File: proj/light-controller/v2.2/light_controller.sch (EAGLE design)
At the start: 214 parts, among them J1 0022232051, J2 PJ-036AH, J4 54602-908LF, J5 A-2004-1-4-LP-N-R, J6 A-2004-1-4-LP-N-R, J7 I2C-HEADER, J8 54602-908LF, U1 RCD-24-0.70/VREF, U10 PCA9685, U11 PCA9615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

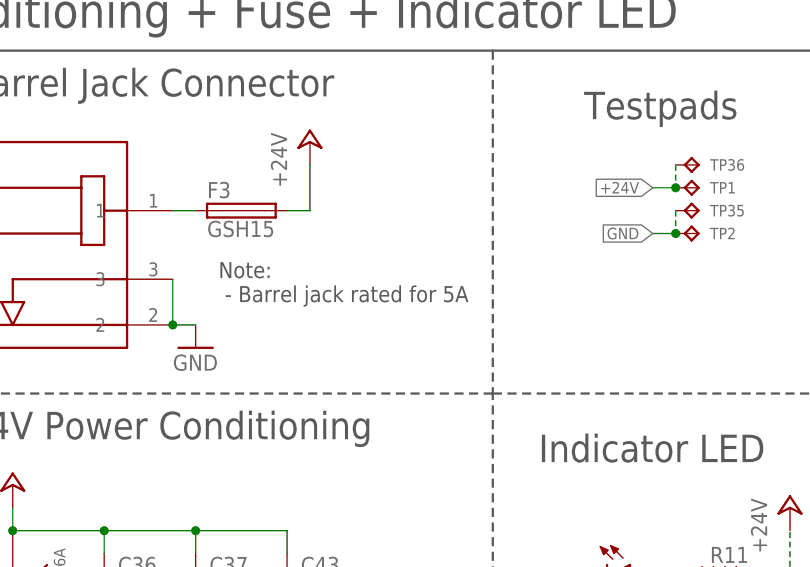
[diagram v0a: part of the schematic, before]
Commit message: added BOM for light controlled v2.2
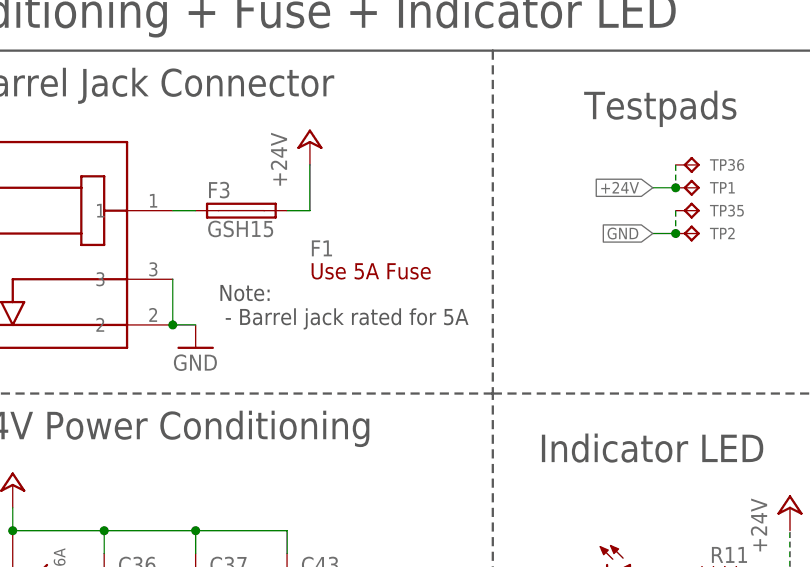
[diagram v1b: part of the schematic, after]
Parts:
- added F1: Use 5A Fuse, openag-fuses:0217005.MXP
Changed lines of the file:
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@@
 <part name="TP37" library="openag-testpads" deviceset="TP" device="TP04R"/>
 <part name="TP38" library="openag-testpads" deviceset="TP" device="TP04R"/>
+<part name="F1" library="openag-fuses" deviceset="0217005.MXP" device="" value="Use 5A Fuse"/>
 </parts>
 <sheets>
@@
 <text x="657.86" y="259.08" size="3.048" layer="97">Testpads</text>
 <wire x1="647.7" y1="266.7" x2="647.7" y2="228.6" width="0.254" layer="97" style="longdash"/>
-<text x="617.22" y="238.76" size="1.778" layer="97">Note:
+<text x="617.22" y="236.22" size="1.778" layer="97">Note:
  - Barrel jack rated for 5A</text>
 <wire x1="266.7" y1="419.1" x2="266.7" y2="342.9" width="0.254" layer="97"/>
@@
 <instance part="TP37" gate="G$1" x="515.62" y="358.14" rot="R180"/>
 <instance part="TP38" gate="G$1" x="515.62" y="363.22" rot="R180"/>
+<instance part="F1" gate="G$1" x="632.46" y="241.3"/>
 </instances>
 <busses>

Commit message: added auto map generation script and applied to light controlled v2.2
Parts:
- U$7: URL https://github.com/openaginitiative/openag_eagle/proj/light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 -> github.com/openaginitiative/openag_eagle/proj/light-control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
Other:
- note added: "Changelog - added particle photon"
- note added: "RJ45 Connector Pair w/dI2C Redriver"
- note removed: "Changelog - added psoc4100"
- note removed: "RJ45 Connector Pair w/dI2C Buffer"
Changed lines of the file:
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@@
 <setting verticaltext="up"/>
 </settings>
-<grid distance="0.1" unitdist="inch" unit="inch" style="lines" multiple="1" display="yes" altdistance="0.01" altunitdist="inch" altunit="inch"/>
+<grid distance="1.5" unitdist="inch" unit="inch" style="lines" multiple="1" display="yes" altdistance="0.01" altunitdist="inch" altunit="inch"/>
 <layers>
 <layer number="1" name="Top" color="4" fill="1" visible="no" active="no"/>
@@
 <part name="U$7" library="openag-frames" deviceset="TITLE" device="">
 <attribute name="TITLE" value="Light Controller"/>
-<attribute name="URL" value="https://github.com/openaginitiative/openag_eagle/proj/light-controller"/>
+<attribute name="URL" value="github.com/openaginitiative/openag_eagle/proj/light-controller"/>
 <attribute name="VER" value="2.2"/>
 </part>
@@
 <text x="38.1" y="307.34" size="3.81" layer="97">6-Channel 24V, 700mA (per channel) Current Regulator Module w/I2C Controlled Dimming via PWM or Analog Signaling</text>
 <text x="580.136" y="39.116" size="3.81" layer="97">Changelog
-- added psoc4100</text>
+- added particle photon</text>
 <wire x1="723.9" y1="0" x2="0" y2="0" width="0.254" layer="94"/>
 <wire x1="0" y1="0" x2="0" y2="457.2" width="0.254" layer="94"/>
@@
 <wire x1="38.1" y1="342.9" x2="76.2" y2="342.9" width="0.1524" layer="97"/>
 <text x="60.96" y="411.48" size="3.048" layer="103">Linear Regulator</text>
-<text x="381" y="231.14" size="3.81" layer="103">RJ45 Connector Pair w/dI2C Buffer</text>
+<text x="381" y="231.14" size="3.81" layer="103">RJ45 Connector Pair w/dI2C Redriver</text>
 <wire x1="76.2" y1="342.9" x2="114.3" y2="342.9" width="0.1524" layer="97"/>
 <wire x1="381" y1="114.3" x2="381" y2="190.5" width="0.254" layer="97"/>
